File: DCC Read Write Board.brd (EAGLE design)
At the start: 85.6 x 57.3 mm, 60 parts, among them IC5 4163D, K1 68613014122, K2 686318124422, Q181 744053D, Q182 74HCT175D, Q183 74HC00D, U185 74HC02D

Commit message: Most of the Write amp and logic gate schematic done
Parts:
- removed K2: 686318124422, FPC_Connectors_Flat_Flexible_Cable_rev15c:686318124422
- added C133, C134, C138, C151, C181, C183: 100nF, rcl:C0603
- added C135, C137, C148, C150: 68uF 10V, rcl:153CLV-0405
- added J103: 686318124422, FPC_Connectors_Flat_Flexible_Cable_rev15c:686318124422
- added Q1: MUN2211T1, transistor-npn:SC59-BEC
- added Q102, Q103, Q180: 2SC2712GR, transistor-npn:SOT23-BEC
- added Q104: 2SD99CL, transistor-npn:SOT23-BEC
- added R1, R2: 560R, rcl:R0603
- added R151: 12R, rcl:R0603
- added R155: 2K2, rcl:R0603
- added R156: 220R, rcl:R0603
- added R167: 100R, pot-vitrohm:PC25
- added R180: 1K, rcl:R0603
- added R181: 330R, rcl:R0603
- added R182: 10R, rcl:R0603
- added R183: 12K, rcl:R0603
- added R184: 47R, rcl:R0603
- added R185: 1K8, rcl:R0603
- added R186: 68R, rcl:R0603
- added R187: (no value), ptc-ntc:P640
- C2, C3: value 100nF -> 1uF
- moved C2 52.3 mm to (80.6, -19.8)
- moved C3 52.3 mm to (85.6, -19.8)
- moved IC5 4.93 mm to (72.4, 48.4)
- renumbered C10 to C152, C5 to C185, U$1 to Q101, U$2 to Q151
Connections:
- new net +8V: C133.1, C148.+, J103.14, Q102.C, Q103.C, Q104.C, R1.2
- new net 1: J103.1
- new net 10: J103.10
- new net 12: J103.12
- new net 3: J103.3
- new net 4: J103.4
- new net 5: J103.5
- new net 6: J103.6
- new net 8: J103.8
- new net ANA_L: J103.18
- new net ANA_R: J103.16
- new net CC/!DCC: J103.13, Q1.B
- new net N$11: IC5.9, Q181.10, Q183.8
- new net N$12: Q181.5, Q182.2, Q183.10
- new net N$13: IC5.15, Q181.11, Q182.13, Q183.2, U185.5
- new net N$14: Q181.15, Q182.5
- new net N$15: Q181.9, Q183.3
- new net N$16: Q182.6, Q183.1
- new net N$17: Q182.15, U185.6
- new net N$18: U185.11, U185.4, U185.9
- new net N$28: Q181.3, Q182.10, U185.3
- new net N$29: Q181.1, Q181.14
- new net N$39: Q181.12, Q182.7, U185.2
- new net N$40: U185.1, U185.8
- new net N$41: Q182.11, U185.12
- new net N$42: Q181.4, Q182.12
- new net N$43: R183.1, U185.10
- new net N$44: Q1.C, Q101.9
- new net N$45: R180.1, U185.13
- new net N$46: Q180.B, R180.2, R181.2
- new net N$47: Q180.E, R182.2
- new net N$48: Q151.11, R156.2, R167.E, R167.S
- new net N$49: Q151.12, R155.2, R167.A
- new net N$50: Q151.8, R151.2
- new net N$51: Q102.E, Q103.B, Q104.B
- new net N$52: C137.+, C138.1, Q102.B, R1.1, R2.2
- new net R184_END: R184.1, R185.1, R186.2, R187.1
- new net RD_LCK: J103.9
- new net RD_MUX: J103.7
- new net RD_SYNK: J103.11
- new net SENSE_GND: Q151.9, R183.2, R184.2
- new net SOURCE: Q151.6, Q180.C
- new net VSENSE_2: C3.1, Q103.E
- net +5V: now also C134.1, C135.+, C150.+, C151.1, C181.1, C183.1, IC5.1, J103.15, Q151.10, Q151.4, Q181.13, Q182.1, R151.1, R185.2; no longer C2.1, C3.1
- net GND: now also C133.2, C134.2, C135.-, C137.-, C138.2, C148.-, C150.-, C151.2, C181.2, C183.2, J103.17, J103.2, Q1.E, Q151.3, Q181.2, Q181.6, Q183.4, Q183.5, R155.1, R156.1, R181.1, R182.1, R186.1, R187.2, R2.1
- net VSENSE_1: now also C2.1, Q104.E

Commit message: Everything added to schematic, but needs checking
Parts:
- added C102, C113, C114: 1uF 16V, rcl:153CLV-0505
- added C115, C116: 2.2uF 6.3V, rcl:153CLV-0505
- added C117, C118: 1.8nF, rcl:C0603
- added C119, C120, C12???: 10uF 16V, rcl:153CLV-0505
- added C121: 10uF, rcl:153CLV-0505
- added C131, C132: 10nF, rcl:C0603
- added C141, C196: 100nF, rcl:C0603
- added C190, C191: 33nF, rcl:C0603
- added C192: 1000p, rcl:C0603
- added C193: 39p, rcl:C0603
- added C194, C195: 2200p, rcl:C0603
- added J111, J112, J121, J122: PTR1PAD1-17, testpad:P1-17
- added L101, L102: 15uH, rcl:L1812
- added Q106, Q190: 2SC2712GR, transistor-npn:SOT23-BEC
- added R101, R102, R110, R5: 4K7, pot-vitrohm:PC25
- added R103, R104: 47K, rcl:R0603
- added R105, R106: 30K, rcl:R0603
- added R107, R108: 150K, rcl:R0603
- added R111, R112, R113, R114: 10R, rcl:R0603
- added R120: 0R???, rcl:R0603
- added R125: 100K, rcl:R0603
- added R127, R128: 1K, rcl:R0603
- added R136: 39K, rcl:R0603
- added R146, R194, R3, R4: 560R, rcl:R0603
- added R171, R172: 4K7, rcl:R0603
- added R192: 1K8, rcl:R0603
- added R193: 1K5, rcl:R0603
- added R195: 100R, rcl:R0603
- added R196: 27R, rcl:R0603
- added R197, R198: 39R, rcl:R0603
- added R199: 0R?, rcl:R0603
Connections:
- net 1 renamed +5V_WRITE
- new net +5V_READ: J103.15
- new net INMF_L: C117.2, Q101.33, R103.1, R105.1, R107.2
- new net INMF_R: C118.2, Q101.24, R104.1, R106.1, R108.2
- new net IN_L: C119.-, Q101.31
- new net IN_R: C120.-, Q101.26
- new net MFL_1: Q101.32, R105.2, R113.1, R127.2
- new net MFL_2: Q101.30, R111.1
- new net MFL_3: R106.2, R128.2
- new net MFL_A: C190.1, R113.2
- new net MFL_B: L101.1, R197.1
- new net MFR_1: Q101.25, R114.1
- new net MFR_2: Q101.27, R112.1
- new net MFR_A: C191.1, R114.2
- new net MFR_B: L102.1, R198.1
- new net MUXAUX: Q101.2
- new net N$53: C102.-, Q101.10
- new net N$54: C141.2, Q101.1
- new net N$55: Q101.7, R136.1
- new net N$56: C141.1, R125.2, R136.2
- new net N$57: C12???.+, Q101.22
- new net N$58: C192.1, Q183.11
- new net N$59: C192.2, R192.1
- new net N$60: C196.1, R193.2, R195.2, R199.1
- new net N$61: C193.1, Q190.B, R192.2, R193.1, R194.2
- new net N$62: C194.1, C195.1, Q190.C, R195.1
- new net N$63: Q190.E, R196.2
- new net N$64: C195.2, R198.2
- new net N$65: C194.2, R197.2
- new net N$66: L102.2, R112.2
- new net N$67: L101.2, R111.2
- new net N$68: J122.TP, Q101.44
- new net N$69: J121.TP, Q101.37
- new net N$70: J111.TP, R120.1, R146.2
- new net N$71: C115.-, R101.S
- new net N$72: C116.-, R102.S
- new net N$73: C115.+, R103.2
- new net N$74: C116.+, R104.2
- new net N$76: C117.1, R127.1
- new net N$77: R107.1, R5.S
- new net N$79: C118.1, R128.1
- new net N$80: R108.1, R110.S
- new net N$81: R171.2, R5.A
- new net N$82: R110.A, R172.2
- new net OUT_L: C113.+, Q101.34
- new net OUT_R: C114.+, Q101.23
- new net RDCLK: Q101.6
- new net RDMUX: Q101.3
- new net RDSYNC: Q101.5
- new net REF_4: C121.-, Q101.35
- net +5V: now also C102.+, C121.+, Q183.13, R110.E, R199.2, R5.E; no longer J103.15
- net ANA_L: now also C113.-, R101.A
- net ANA_R: now also C114.-, R102.A
- net BIAS1: now also J112.TP, R146.1
- net GND: now also C12???.-, C131.2, C132.2, C190.2, C191.2, C193.2, C196.2, R101.E, R102.E, R125.1, R171.1, R172.1, R194.1, R196.1
- net MRH_L: now also C119.+, C131.1, R4.1
- net MRH_R: now also C120.+, C132.1, R3.1
- net VSENSE_1: now also R120.2
- net VSENSE_2: now also R3.2, R4.2

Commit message: Schematic complete. Still needs checking
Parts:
- added C143: 4.7uF 16V, rcl:153CLV-0505
- added Q2: BCX71SMD, transistor-pnp:SOT23
- added R129: 47R, rcl:R0603
- added R130: 470R, rcl:R0603
- added R131: 330R, rcl:R0603
- added R132: 560R, rcl:R0603
- added R133: 8K2, rcl:R0603
- added R134: 12K, rcl:R0603
- added R135: 1K, pot-vitrohm:PC25
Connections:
- removed net +5V: C1.1, C102.+, C121.+, C134.1, C135.+, C150.+, C151.1, C152.2, C181.1, C183.1, C185.1, C4.1, IC5.1, IC5.10, IC5.16, IC5.3, IC5.6, IC5.7, Q101.21, Q101.36, Q101.4, Q151.10, Q151.19, Q151.4, Q181.13, Q181.16, Q182.1, Q182.16, Q183.13, Q183.14, R110.E, R151.1, R185.2, R199.2, R5.E, U185.14
- removed net 10: J103.10
- removed net 12: J103.12
- removed net 3: J103.3
- removed net 4: J103.4
- removed net 5: J103.5
- removed net 6: J103.6
- removed net 8: J103.8
- removed net RDCLK: Q101.6
- removed net RDSYNC: Q101.5
- removed net RD_LCK: J103.9
- removed net RD_SYNK: J103.11
- removed net WCLOCK: IC5.2, Q151.1, Q182.9
- new net N$75: C143.-, Q106.B, R133.2, R134.1
- new net N$78: Q106.E, R130.1, R131.2
- new net N$83: Q106.C, Q2.1, R132.1
- new net N$84: Q2.3, R129.1, R130.2
- new net N$85: C143.+, R135.S
- new net RD_SYNC: J103.11, Q101.5
- new net WCLCK: IC5.2, J103.3, Q151.1, Q182.9
- net +5V_READ: now also C102.+, C121.+, C134.1, C135.+, Q101.21, Q101.36, Q101.4, Q2.2, R110.E, R132.2, R134.2, R199.2, R5.E
- net +5V_WRITE: now also C1.1, C150.+, C151.1, C152.2, C181.1, C183.1, C185.1, C4.1, IC5.1, IC5.10, IC5.16, IC5.3, IC5.6, IC5.7, Q151.10, Q151.19, Q151.4, Q181.13, Q181.16, Q182.1, Q182.16, Q183.13, Q183.14, R151.1, R185.2, U185.14
- net GND: now also J103.10, J103.12, J103.4, J103.6, J103.8, R131.1, R133.1, R135.A
- net RDMUX: now also R135.E
- net RD_CLCK: now also J103.9, Q101.6
- net RD_MUX: now also R129.2
- net WDATA: now also J103.5
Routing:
- net +5V_WRITE: track 0.00 -> 11.7 mm
- net +5V: track 11.7 -> 0.00 mm

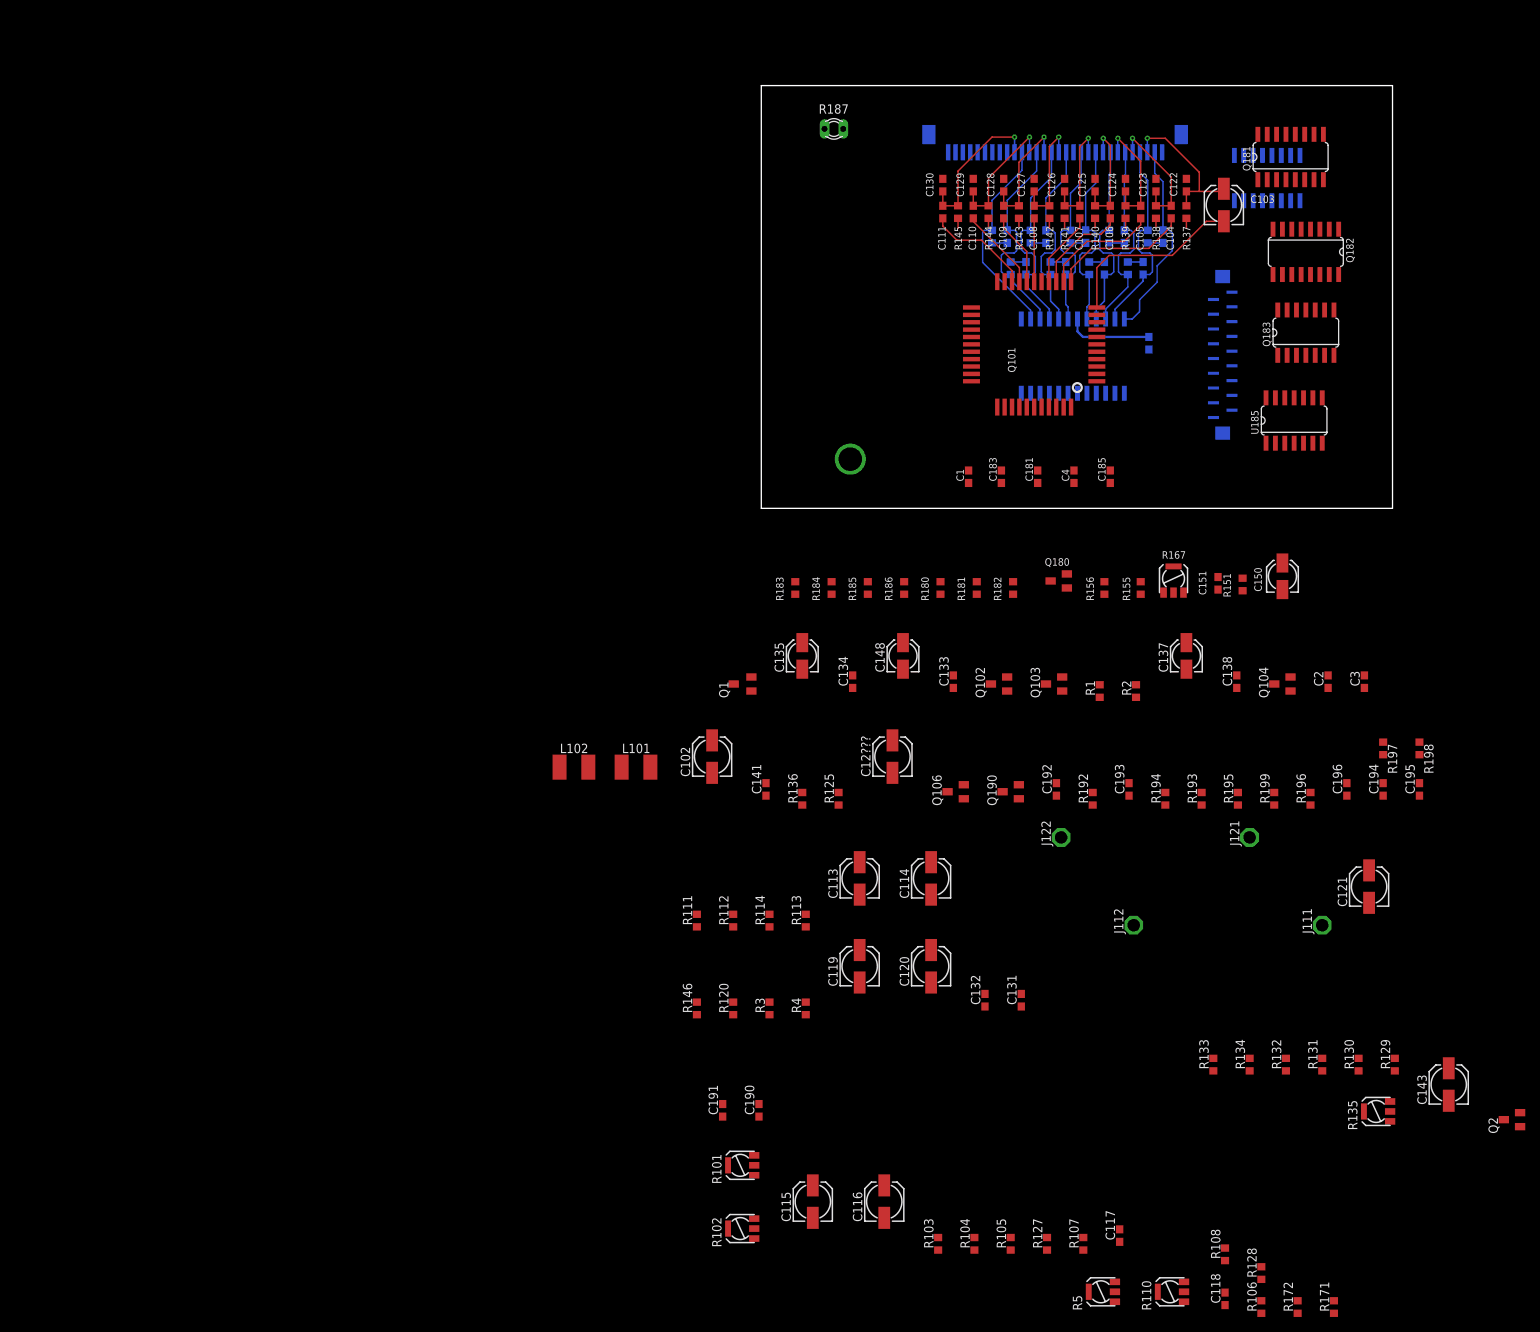
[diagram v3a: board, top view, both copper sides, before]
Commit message: Started placing more passives
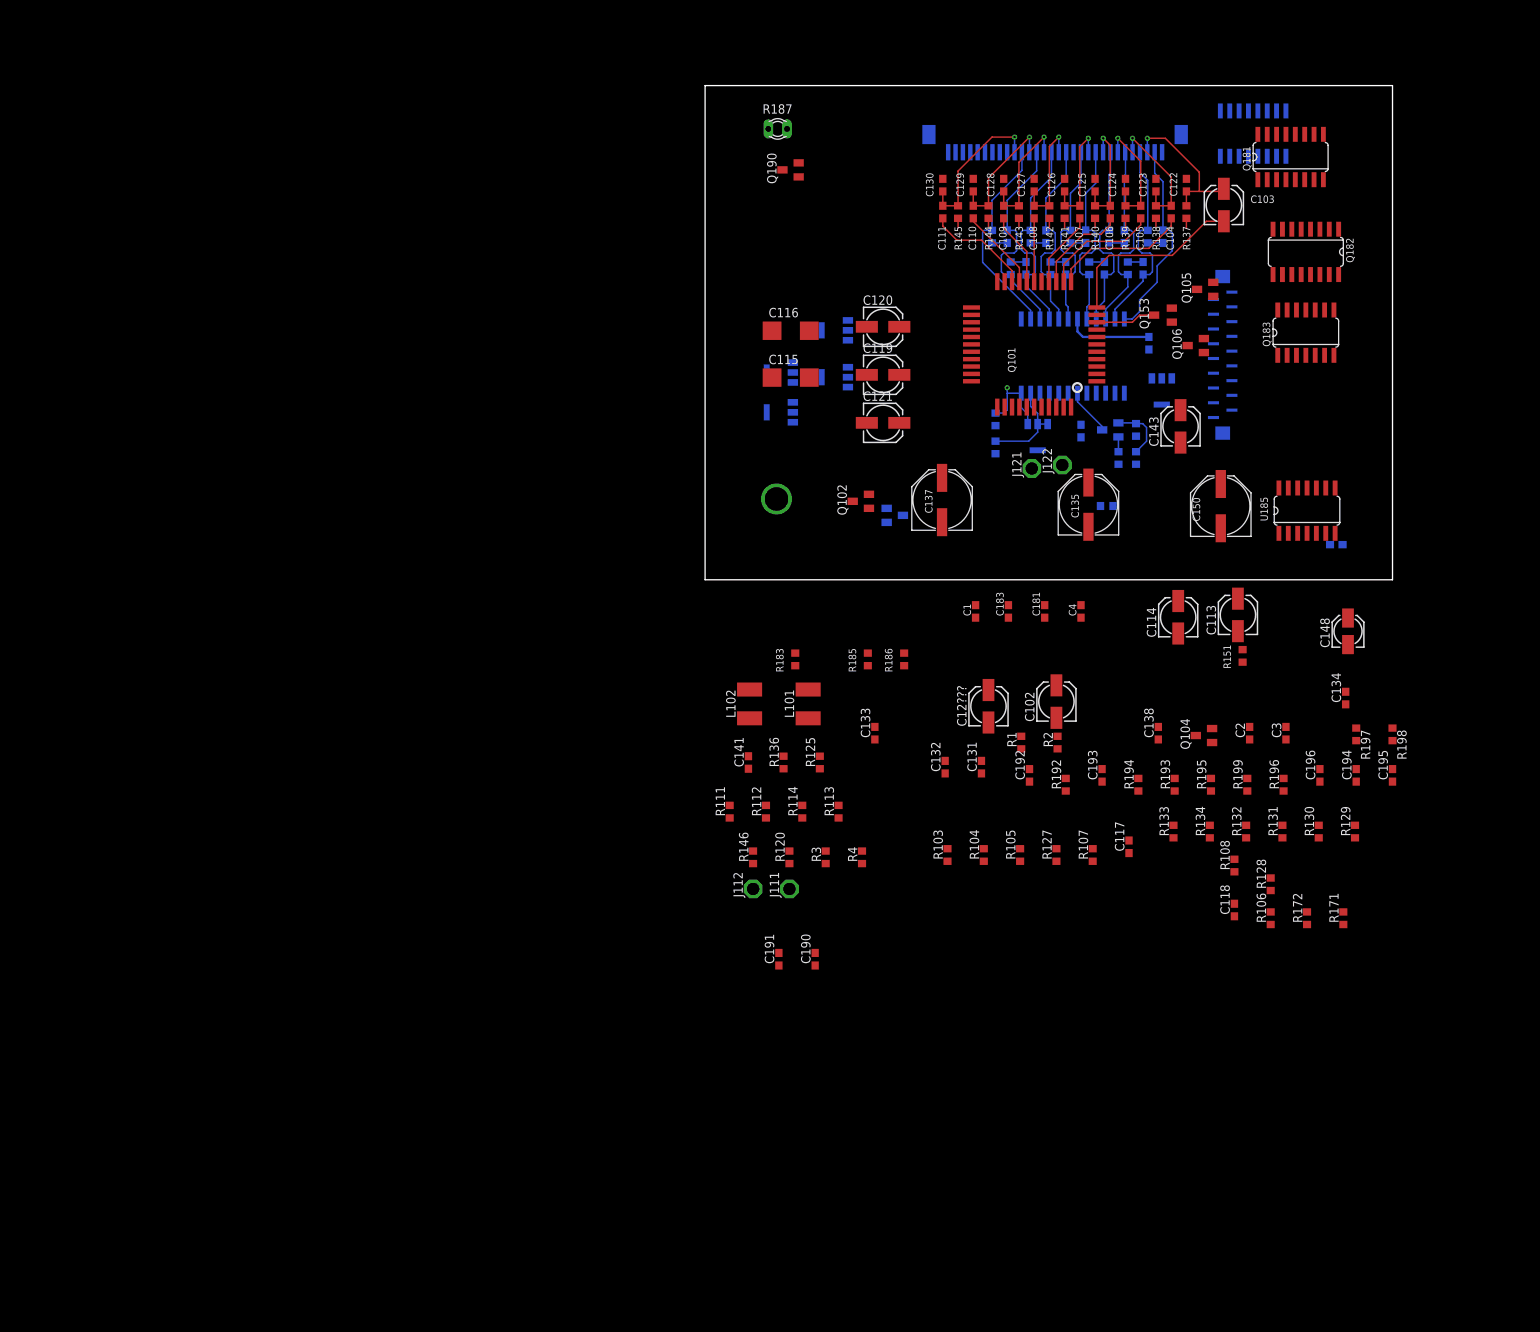
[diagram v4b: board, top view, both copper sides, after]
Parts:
- removed Q1: MUN2211T1, transistor-npn:SC59-BEC
- removed Q2: BCX71SMD, transistor-pnp:SOT23
- removed R5: 4K7, pot-vitrohm:PC25
- added Q105: BCX71SMD, transistor-pnp:SOT23
- added Q153: MUN2211T1, transistor-npn:SC59-BEC
- added R109: 4K7, pot-vitrohm:PC25
- C115, C116: device rcl:153CLV-0505 -> rcl:C/6032-28R
- C135, C137, C150: device rcl:153CLV-0405 -> rcl:PANASONIC_E
- moved R110 135.4 mm to (6.19, 22.1), flipped to the bottom, turned to 270 degrees
- moved R102 122.4 mm to (13.7, 27.8), flipped to the bottom, turned to 270 degrees
- moved C116 118.7 mm to (7.79, 27.7), turned to 0 degrees
- moved C115 111.7 mm to (7.79, 21.4), turned to 0 degrees
- moved R101 107.6 mm to (13.7, 21.4), flipped to the bottom, turned to 270 degrees
- moved R135 101.7 mm to (58.1, 19.4), flipped to the bottom, turned to 180 degrees
- moved C143 96.3 mm to (60.6, 14.8)
- moved C121 91.1 mm to (20.3, 15.2), turned to 0 degrees
- moved Q190 89.4 mm to (7.78, 49.5)
- moved C120 86.9 mm to (20.3, 28.3), turned to 0 degrees
- moved C119 80.2 mm to (20.3, 21.7), turned to 0 degrees
- moved J111 72.4 mm to (7.62, -47.9)
- moved Q106 68.7 mm to (62.7, 25.7)
- moved C134 66.9 mm to (83.0, -22.1)
- moved C113 62.5 mm to (68.4, -10.8)
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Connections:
- net +5V_READ: now also Q105.2, R109.E; no longer Q2.2, R5.E
- net CC/!DCC: now also Q153.B; no longer Q1.B
- net GND: now also Q153.E; no longer Q1.E
- net N$44: now also Q153.C; no longer Q1.C
- net N$77: now also R109.S; no longer R5.S
- net N$81: now also R109.A; no longer R5.A
- net N$83: now also Q105.1; no longer Q2.1
- net N$84: now also Q105.3; no longer Q2.3
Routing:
- net N$48: track 0.00 -> 13.3 mm
- net N$49: track 0.00 -> 11.2 mm, vias 0 -> 1
- net N$44: track 0.00 -> 8.16 mm
- net N$46: track 0.00 -> 7.95 mm
- net SOURCE: track 0.00 -> 6.36 mm
- net N$47: track 0.00 -> 2.01 mm
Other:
- board size 85.6 x 57.3 mm -> 93.2 x 67 mm
